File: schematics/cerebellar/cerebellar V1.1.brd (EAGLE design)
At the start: 98.4 x 91.1 mm, 68 parts, among them CON1 ODRV2, CON2 ODRV1, CON3 ODRV3, CON4 ODRV4, CON5 ODRV5, CON6 ODRV6, IC3 LTC7001, P1 Foot1, P10 SPI2, P11 Foot2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

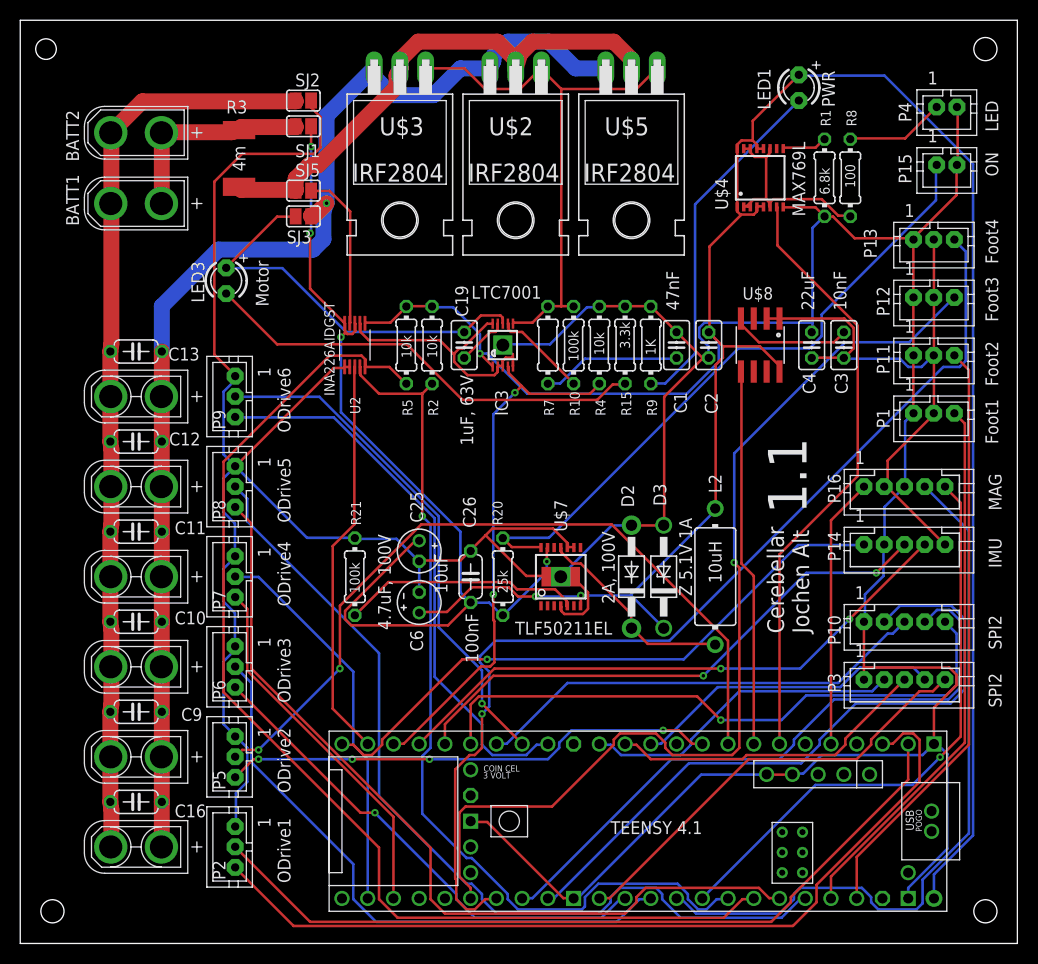
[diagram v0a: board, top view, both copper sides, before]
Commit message: Schematics with power supply and INA works
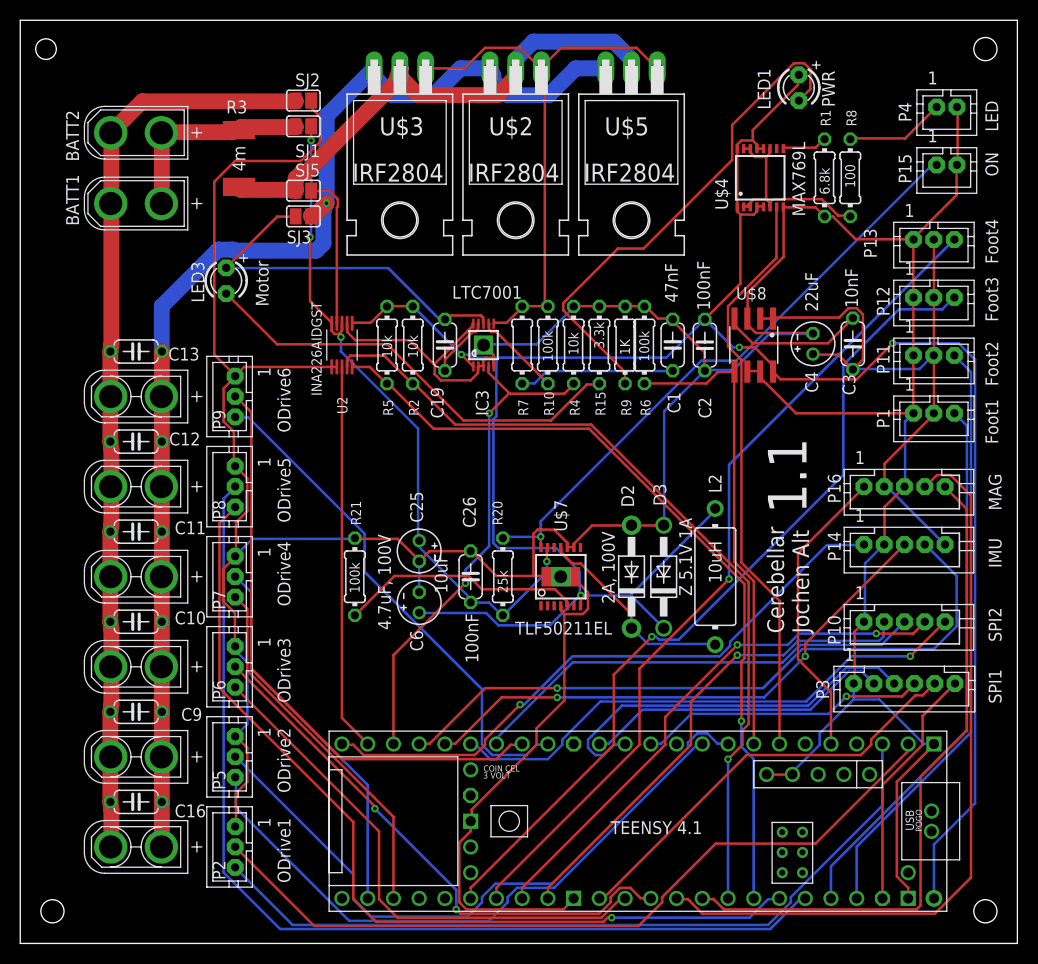
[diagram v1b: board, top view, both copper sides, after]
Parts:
- added R6: 100k, rcl:0204/7
- C1, C19, C2, C3: device rcl:C025-025X050 -> rcl:C050-024X044
- C4: device rcl:C025-025X050 -> rcl:E2-4
- P3: value SPI2 -> SPI1; device jst-ph:JST-PH5 -> jst-ph:JST-PH6
- moved R15 2.54 mm to (50.8, 59.1)
- moved R10 2.54 mm to (45.7, 59.1)
- moved R4 2.54 mm to (48.3, 59.1)
- moved R7 2.54 mm to (43.2, 59.1)
- moved R9 2.54 mm to (53.3, 59.1)
- moved C19 1.91 mm to (35.6, 59.1)
- moved IC3 1.91 mm to (39.4, 59.1)
- moved R2 1.91 mm to (32.4, 59.1)
- moved R5 1.91 mm to (29.8, 59.1)
- moved U2 1.27 mm to (25.4, 59.1)
- moved P3 1.09 mm to (80.9, 25.7)
- moved C3 0.90 mm to (75.8, 59.2)
- moved U$8 0.63 mm to (66.0, 59.1)
- moved C1 0.38 mm to (58.0, 59.1)
- moved C2 0.38 mm to (61.2, 59.1)
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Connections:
- removed net N$9: U$1.6-OUT1D, U$8.5
- new net SHDN: R6.1, U$1.6-OUT1D, U$8.5
- net +3.3V: now also C4.+; no longer C4.1
- net GND: now also C4.-, R6.2, U$8.3, U$8.6, U$8.7; no longer C4.2
- net N$7: now also P3.6
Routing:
- net SHDN: track 0.00 -> 47.0 mm
- net N$9: track 37.3 -> 0.00 mm
- net N$17: track 112.1 -> 79.3 mm, vias 0 -> 1
- net V+: track 92.8 -> 67.3 mm
- net N$7: track 0.00 -> 24.2 mm
- net SENS4: track 103.4 -> 83.7 mm
- net MISO1: track 66.1 -> 48.4 mm, vias 0 -> 1
- net N$39: track 34.8 -> 50.5 mm
- net SENS3: track 98.9 -> 83.6 mm
- net O2_TX: track 48.9 -> 61.3 mm, vias 4 -> 0
- net O5_RX: track 87.3 -> 99.6 mm
- net O2_RX: track 76.7 -> 65.1 mm, vias 2 -> 0
- net GND: track 435.8 -> 446.6 mm
- net +5V: track 241.6 -> 231.5 mm, vias 3 -> 4
- net CS1: track 63.2 -> 53.3 mm, vias 0 -> 2
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
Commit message: MOSFET Driver tested
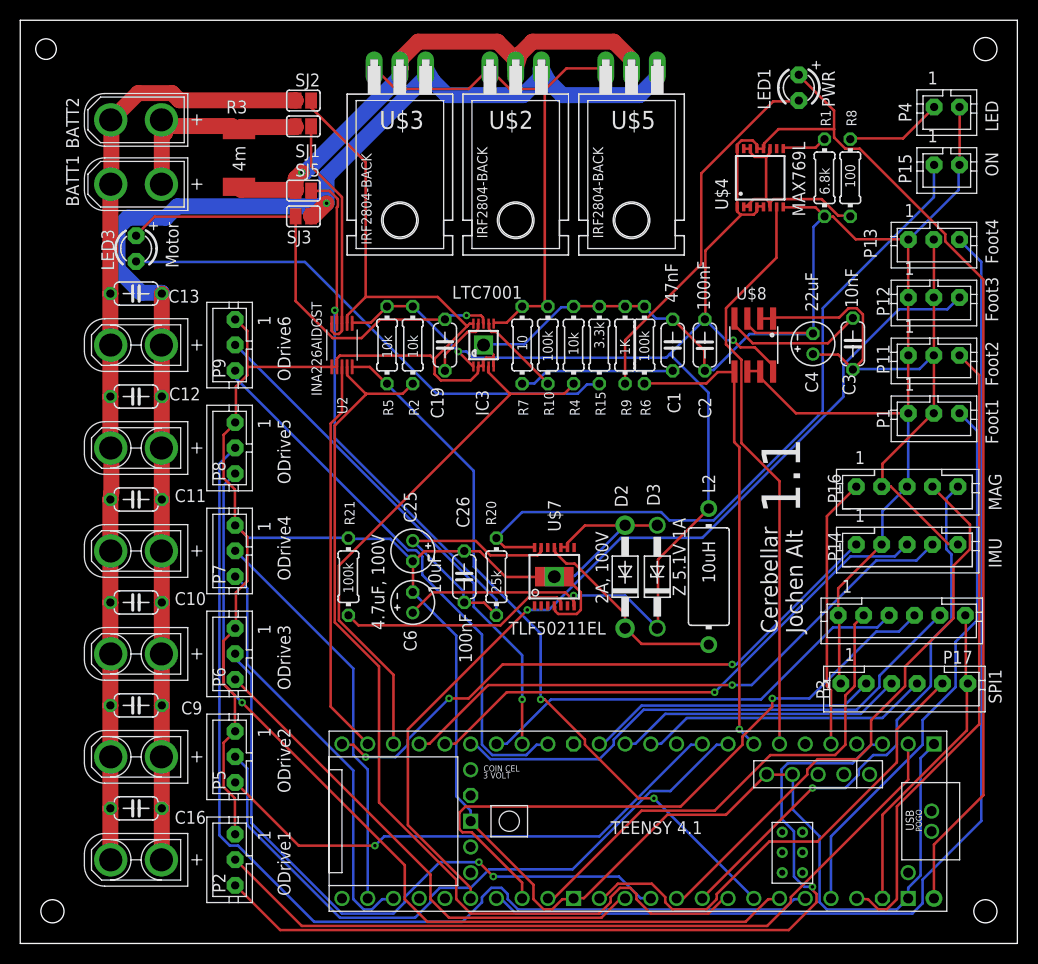
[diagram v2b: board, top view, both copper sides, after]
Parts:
- removed P10: SPI2, jst-ph:JST-PH5
- added P17: SPI2, jst-ph:JST-PH6
- U$2, U$3, U$5: value IRF2804 -> IRF2804-BACK; device IRF2804:TO-220H -> IRF2804:TO-220H-BACK
- moved LED3 9.44 mm to (5.08, 68.6)
- moved C13 5.72 mm to (5.08, 64.1)
- moved CON6 5.08 mm to (5.08, 59.1)
- moved P9 5.08 mm to (13.3, 59.1)
- moved C12 4.45 mm to (5.08, 54.0)
- moved CON5 3.81 mm to (5.08, 48.9)
- moved P8 3.81 mm to (13.3, 48.9)
- moved C11 3.17 mm to (5.08, 43.8)
- moved CON4 2.54 mm to (5.08, 38.7)
- moved P7 2.54 mm to (13.3, 38.7)
- moved BATT1 1.91 mm to (5.08, 74.9)
- moved C10 1.91 mm to (5.08, 33.7)
- moved CON2 1.27 mm to (5.08, 8.26)
- moved CON3 1.27 mm to (5.08, 28.6)
- moved P2 1.27 mm to (13.3, 8.26)
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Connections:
- net N$10 renamed INP
- net N$26 renamed TS
- net N$4 renamed TGUP
- removed net N$18: SJ5.1, U2.9
- removed net N$7: P3.6, U$1.3V3-3
- new net N$9: P17.6, P3.6, U$1.3V3-3
- new net PMS+: C25.+, C26.1, R20.1, SJ5.1, U$7.13, U2.9
- net CS1: now also P17.4; no longer P10.4
- net GATE: now also U$2.3, U$3.3, U$5.3; no longer U$2.1, U$3.1, U$5.1
- net GND: now also P17.1; no longer P10.1
- net MISO1: now also P17.2; no longer P10.2
- net MOSI1: now also P17.3; no longer P10.3
- net POWER+: now also U$2.1, U$3.1, U$5.1; no longer U$2.3, U$3.3, U$5.3
- net SCK1: now also P17.5; no longer P10.5
- net V+: no longer C25.+, C26.1, R20.1, U$7.13
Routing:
- net PMS+: track 0.00 -> 78.0 mm, vias 0 -> 1
- net V+: track 67.3 -> 23.5 mm, vias 4 -> 0
- net N$9: track 0.00 -> 31.7 mm
- net SENS4: track 83.7 -> 111.9 mm, vias 1 -> 0
- net N$7: track 24.2 -> 0.00 mm
- net MAG_SCL: track 74.8 -> 56.8 mm
- net N$18: track 15.3 -> 0.00 mm
- net N$39: track 50.5 -> 36.5 mm
- net POWER+: track 121.7 -> 135.2 mm
- net N$22: track 81.9 -> 95.4 mm, vias 1 -> 0
- net CS1: track 53.3 -> 65.5 mm, vias 2 -> 1
- net MAG_SDA: track 66.3 -> 54.2 mm, vias 0 -> 1
- net N$47: track 60.0 -> 71.2 mm, vias 1 -> 0
- net MOSI: track 39.1 -> 28.8 mm
- net O3_RX: track 54.2 -> 64.4 mm
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
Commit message: new schematics layout
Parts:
- moved LED1 67.3 mm to (5.08, 68.6)
- moved LED3 8.26 mm to (13.3, 68.6)
- moved C1 4.45 mm to (58.0, 54.6)
- moved C19 4.45 mm to (35.6, 54.6), turned to 270 degrees
- moved C2 4.45 mm to (61.2, 54.6)
- moved C3 4.45 mm to (75.8, 54.7)
- moved C4 4.45 mm to (71.9, 54.7)
- moved IC3 4.45 mm to (39.4, 54.6)
- moved R10 4.45 mm to (45.7, 54.6)
- moved R15 4.45 mm to (50.8, 54.6)
- moved R2 4.45 mm to (32.4, 54.6)
- moved R4 4.45 mm to (48.3, 54.6)
- moved R5 4.45 mm to (29.8, 54.6)
- moved R6 4.45 mm to (55.2, 54.6)
- moved R7 4.45 mm to (43.2, 54.6)
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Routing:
- net N$17: track 71.0 -> 126.8 mm, vias 2 -> 0
- net SENS3: track 93.2 -> 127.2 mm, vias 1 -> 0
- net N$22: track 95.4 -> 67.2 mm, vias 0 -> 3
- net +5V: track 233.6 -> 261.1 mm
- net MOSI1: track 44.0 -> 69.5 mm
- net N$39: track 36.5 -> 57.6 mm
- net O5_RX: track 103.6 -> 86.5 mm, vias 0 -> 1
- net O1_TX: track 86.4 -> 71.0 mm
- net O2_RX: track 65.9 -> 51.2 mm, vias 0 -> 1
- net O5_TX: track 88.8 -> 74.3 mm, vias 1 -> 2
- net O4_RX: track 39.7 -> 50.5 mm
- net GND: track 453.4 -> 463.5 mm
- net N$47: track 71.2 -> 80.8 mm
- net O2_TX: track 52.9 -> 62.5 mm, vias 1 -> 0
- net N$42: track 20.3 -> 26.5 mm
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
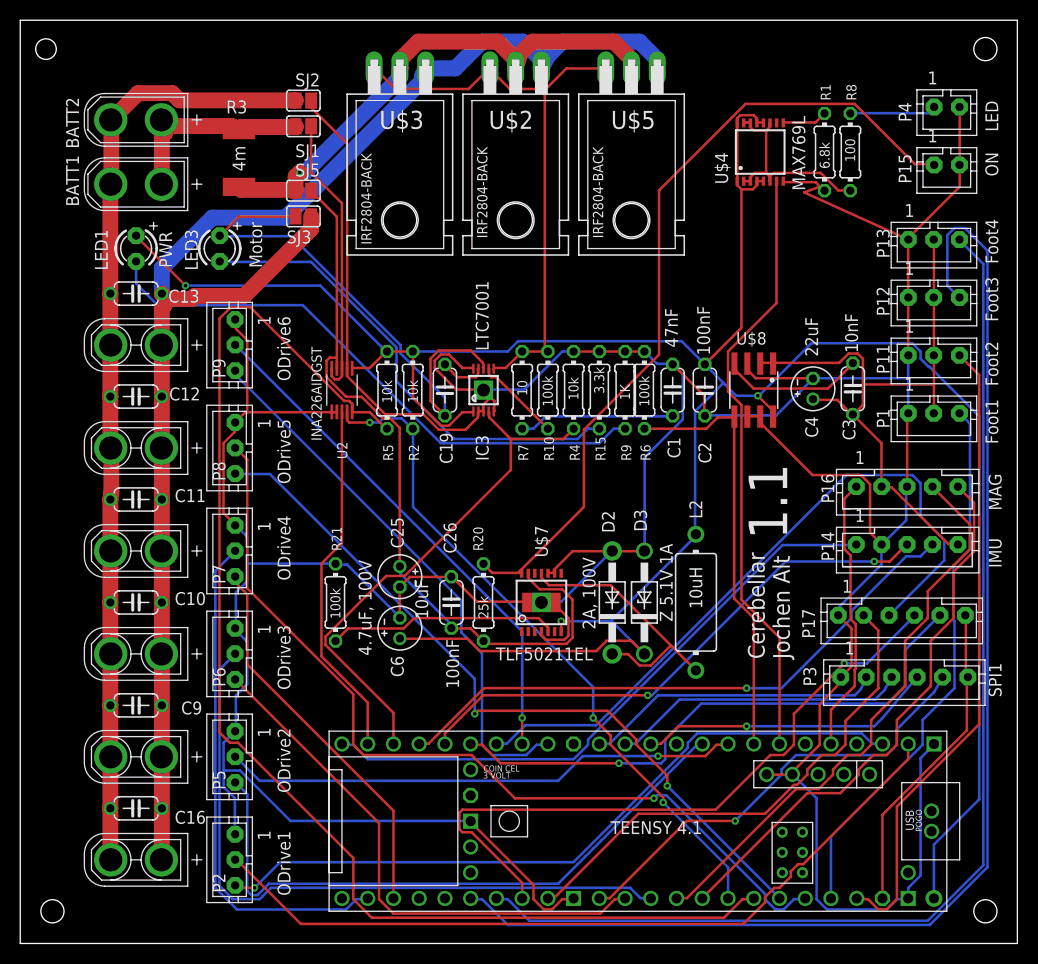
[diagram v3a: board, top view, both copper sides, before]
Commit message: buffersize in UART7 for less checksum errors
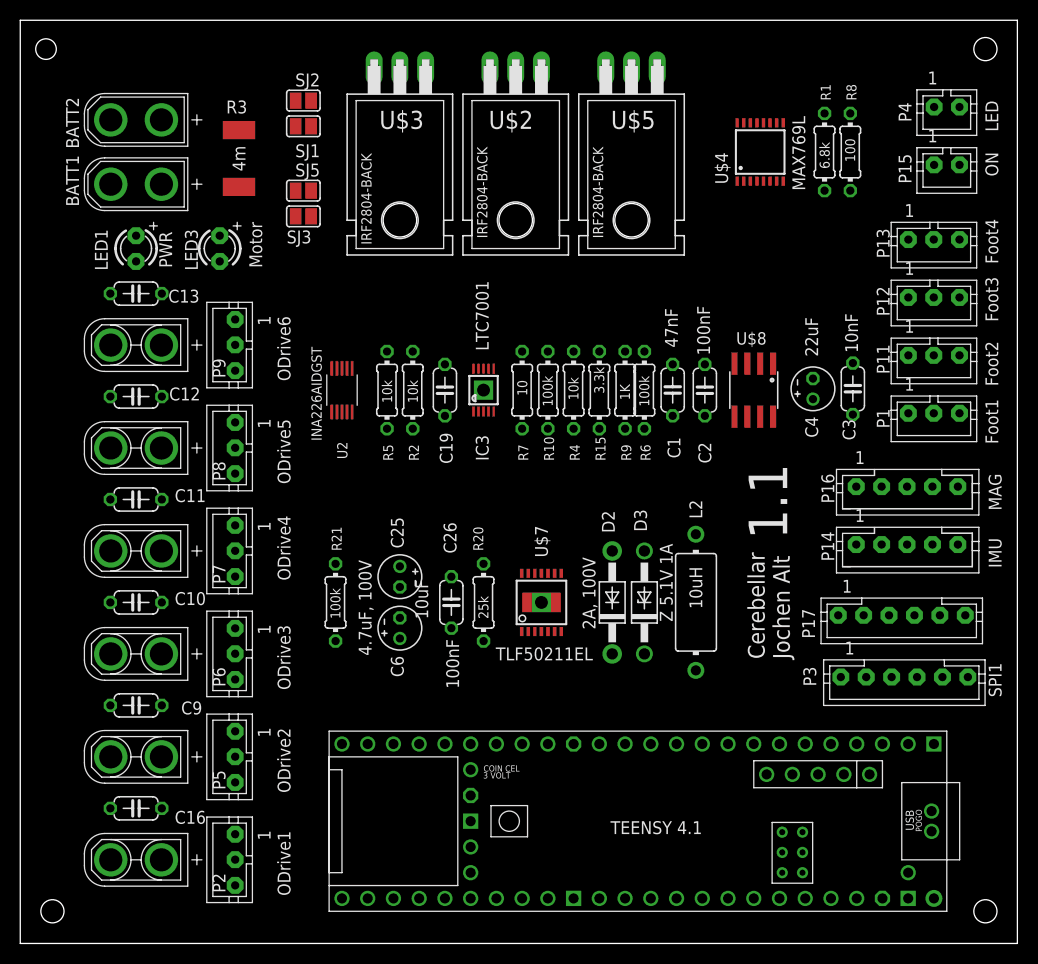
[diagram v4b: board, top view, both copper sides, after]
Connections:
- net N$9 renamed T3.3V
- removed net MAG_EN: U$1.9-OUT1C
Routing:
- net GND: track 463.5 -> 0.00 mm
- net +5V: track 261.1 -> 0.00 mm, vias 3 -> 0
- net POWER+: track 140.3 -> 0.00 mm
- net SENS3: track 127.2 -> 0.00 mm
- net N$17: track 126.8 -> 0.00 mm
- net SENS4: track 114.0 -> 0.00 mm
- net BATT-: track 92.8 -> 0.00 mm
- net O5_RX: track 86.5 -> 0.00 mm, vias 1 -> 0
- net N$47: track 80.8 -> 0.00 mm
- net O1_RX: track 77.9 -> 0.00 mm
- net PMS+: track 74.9 -> 0.00 mm
- net O5_TX: track 74.3 -> 0.00 mm, vias 2 -> 0
- net O1_TX: track 71.0 -> 0.00 mm, vias 1 -> 0
- net MOSI1: track 69.5 -> 0.00 mm
- net O3_RX: track 67.6 -> 0.00 mm
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
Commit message: new layout
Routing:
- net GND: track 0.00 -> 460.7 mm
- net +5V: track 0.00 -> 261.6 mm, vias 0 -> 3
- net POWER+: track 0.00 -> 140.3 mm
- net N$17: track 0.00 -> 126.8 mm
- net SENS4: track 0.00 -> 115.4 mm
- net SENS3: track 0.00 -> 112.6 mm
- net BATT-: track 0.00 -> 92.8 mm
- net O5_RX: track 0.00 -> 91.6 mm
- net O5_TX: track 0.00 -> 81.5 mm, vias 0 -> 1
- net N$47: track 0.00 -> 81.1 mm
- net O1_TX: track 0.00 -> 79.8 mm
- net O1_RX: track 0.00 -> 78.1 mm
- net PMS+: track 0.00 -> 74.9 mm
- net N$22: track 0.00 -> 71.7 mm, vias 0 -> 4
- net +3.3V: track 0.00 -> 63.7 mm
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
